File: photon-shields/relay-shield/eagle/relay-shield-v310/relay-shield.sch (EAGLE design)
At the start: 57 parts, among them J1 POWER_JACKSLT, Q1 MPSA42, Q2 MPSA42, Q3 MPSA42, Q4 MPSA42, U1 RELAYPANASONIC-JS, U2 RELAYPANASONIC-JS, U3 RELAYPANASONIC-JS, U4 RELAYPANASONIC-JS

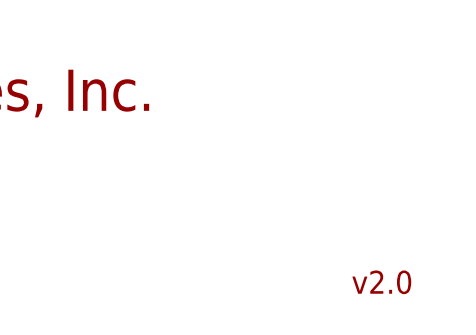
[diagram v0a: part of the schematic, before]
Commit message: added rev numbers to schematic sheets and regenerated the PDFs
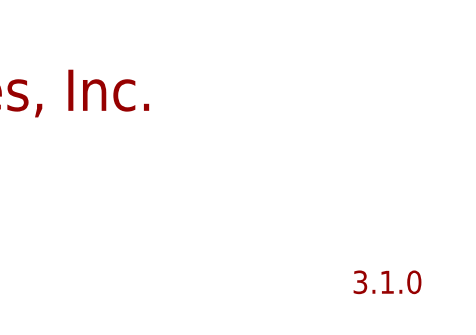
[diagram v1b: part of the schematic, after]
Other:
- note added: "3.1.0"
- note removed: "v2.0"
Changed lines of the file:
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@@
 <text x="8.89" y="66.04" size="7.62" layer="95">Relay Interface</text>
 <text x="193.04" y="66.04" size="7.62" layer="95">Power Supply</text>
-<text x="377.19" y="6.35" size="2.54" layer="94">v2.0</text>
+<text x="377.19" y="6.35" size="2.54" layer="94">3.1.0</text>
 <text x="307.34" y="127" size="1.778" layer="96">6.8uH</text>
 <text x="5.08" y="5.08" size="2.1844" layer="95">Reference Designs ARE PROVIDED "AS IS" AND "WITH ALL FAULTS. PARTICLE INDUSTRIES, INC
